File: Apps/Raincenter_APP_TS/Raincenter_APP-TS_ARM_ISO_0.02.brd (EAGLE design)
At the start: 42.3 x 27.4 mm, 26 parts

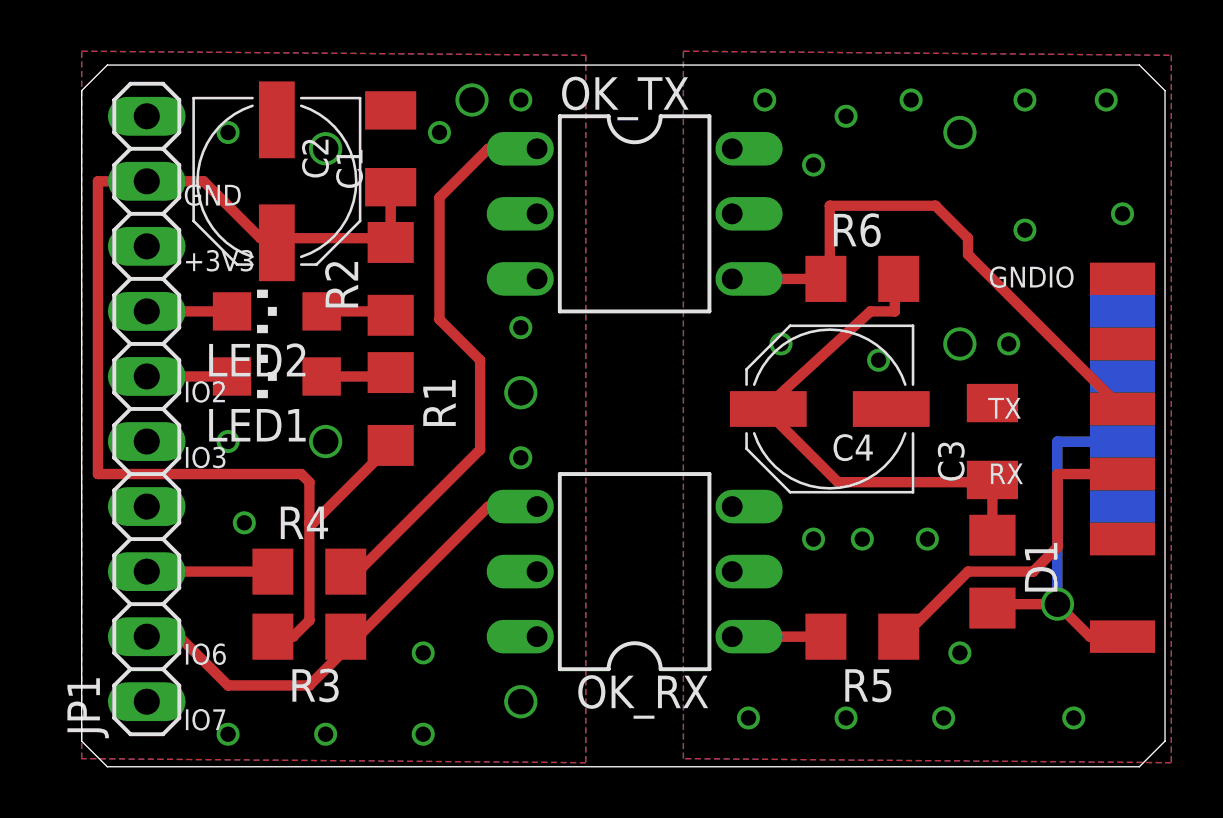
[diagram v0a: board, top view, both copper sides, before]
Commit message: Raincenter_APP: fixed connected CTS instead of RTS, swapped Pin 4&5 of both optokopplers
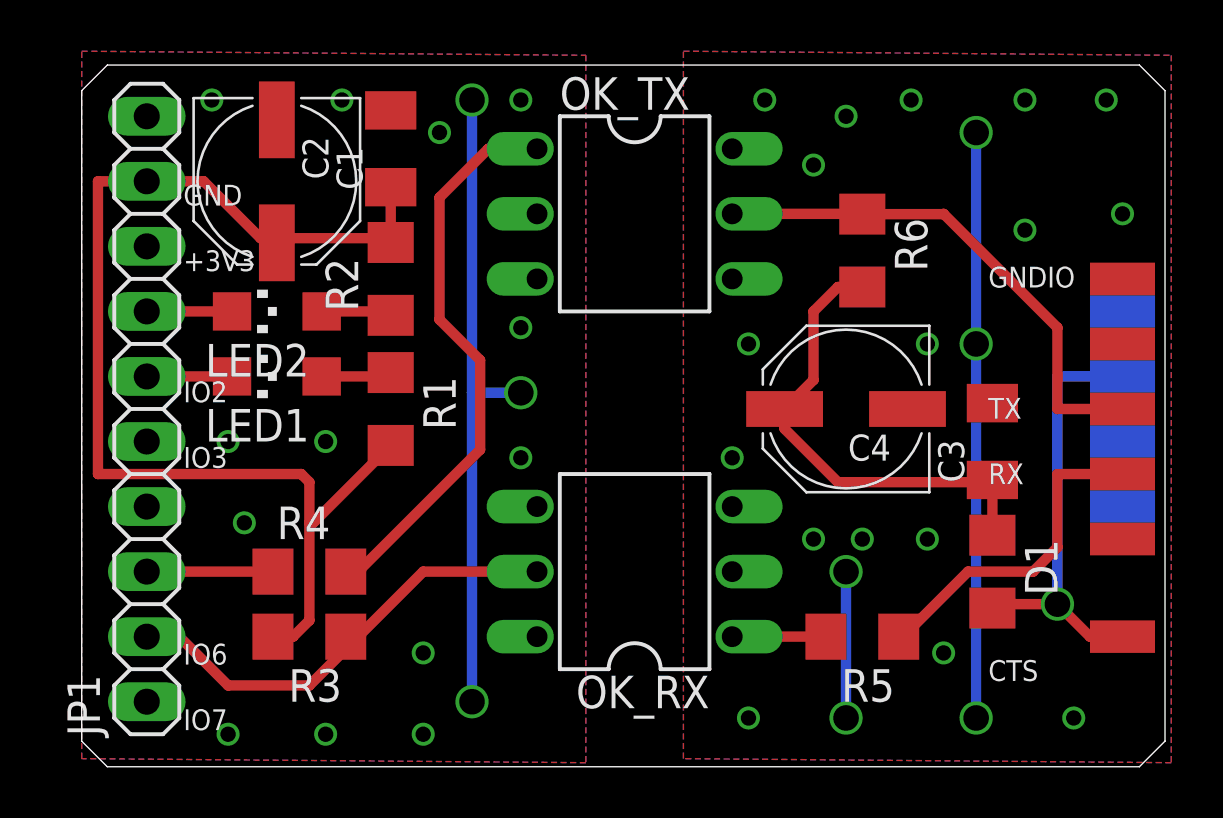
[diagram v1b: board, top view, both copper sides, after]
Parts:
- PAD7: value RTS -> (none)
- PAD8: value (none) -> CTS
- R6: value 2K2 -> 2K7
- moved R6 1.11 mm to (30.5, 20.2), turned to 270 degrees
- moved C4 0.63 mm to (29.8, 14.0)
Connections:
- net GND: now also OK_RX.4; no longer OK_RX.5
- net GNDIO: now also OK_TX.4; no longer OK_TX.5
- net IO7: now also OK_RX.5; no longer OK_RX.4
- net RC_RTS: now also PAD8.1; no longer PAD7.1
- net RX_TX: now also OK_TX.5; no longer OK_TX.4
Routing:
- net GNDIO: track 0.00 -> 28.6 mm, vias 21 -> 22
- net GND: track 0.00 -> 25.4 mm
- net RC_RTS: track 14.6 -> 17.2 mm
- net RX_TX: track 21.8 -> 20.3 mm
- net IO7: track 19.7 -> 18.7 mm
- net V+: track 20.1 -> 19.6 mm
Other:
- board text added: "GNDIO TX RX CTS"
- board text removed: "GNDIO TX RX"
